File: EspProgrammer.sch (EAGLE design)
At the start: 11 parts

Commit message: add documentation
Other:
- note added: "ESP-12"
- note added: "GPIO0 (with Pull-Up) RESET (with Pull-Up) RXD TXD GND"
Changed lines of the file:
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@@
 <setting verticaltext="up"/>
 </settings>
-<grid distance="0.1" unitdist="inch" unit="inch" style="lines" multiple="1" display="no" altdistance="0.01" altunitdist="inch" altunit="inch"/>
+<grid distance="25" unitdist="mil" unit="mil" style="lines" multiple="1" display="no" altdistance="0.01" altunitdist="inch" altunit="inch"/>
 <layers>
 <layer number="1" name="Top" color="4" fill="1" visible="no" active="no"/>
@@
 <wire x1="116.84" y1="106.68" x2="73.66" y2="106.68" width="0.1524" layer="94"/>
 <text x="78.74" y="93.98" size="1.778" layer="94">CP2104 Board</text>
+<wire x1="182.88" y1="114.3" x2="182.88" y2="99.06" width="0.1524" layer="94"/>
+<wire x1="182.88" y1="88.9" x2="182.88" y2="83.82" width="0.1524" layer="94"/>
+<wire x1="182.88" y1="83.82" x2="210.82" y2="83.82" width="0.1524" layer="94"/>
+<text x="185.42" y="110.49" size="1.778" layer="94">ESP-12</text>
+<text x="184.15" y="87.63" size="1.778" layer="94">GPIO0 (with Pull-Up)
+RESET (with Pull-Up)
+RXD
+TXD
+GND</text>
+<wire x1="180.34" y1="99.06" x2="182.88" y2="99.06" width="0.1524" layer="94"/>
+<wire x1="182.88" y1="99.06" x2="182.88" y2="96.52" width="0.1524" layer="94"/>
+<wire x1="180.34" y1="96.52" x2="182.88" y2="96.52" width="0.1524" layer="94"/>
+<wire x1="182.88" y1="96.52" x2="182.88" y2="93.98" width="0.1524" layer="94"/>
+<wire x1="180.34" y1="93.98" x2="182.88" y2="93.98" width="0.1524" layer="94"/>
+<wire x1="182.88" y1="93.98" x2="182.88" y2="91.44" width="0.1524" layer="94"/>
+<wire x1="180.34" y1="91.44" x2="182.88" y2="91.44" width="0.1524" layer="94"/>
+<wire x1="182.88" y1="91.44" x2="182.88" y2="88.9" width="0.1524" layer="94"/>
+<wire x1="182.88" y1="88.9" x2="180.34" y2="88.9" width="0.1524" layer="94"/>
+<wire x1="182.88" y1="114.3" x2="210.82" y2="114.3" width="0.1524" layer="94"/>
+<wire x1="210.82" y1="114.3" x2="210.82" y2="83.82" width="0.1524" layer="94"/>
 </plain>
 <instances>
@@
 </drawing>
 <compatibility>
+<note version="6.3" minversion="6.2.2" severity="warning">
+Since Version 6.2.2 text objects can contain more than one line,
+which will not be processed correctly with this version.
+</note>
 <note version="8.2" severity="warning">
 Since Version 8.2, EAGLE supports online libraries. The ids

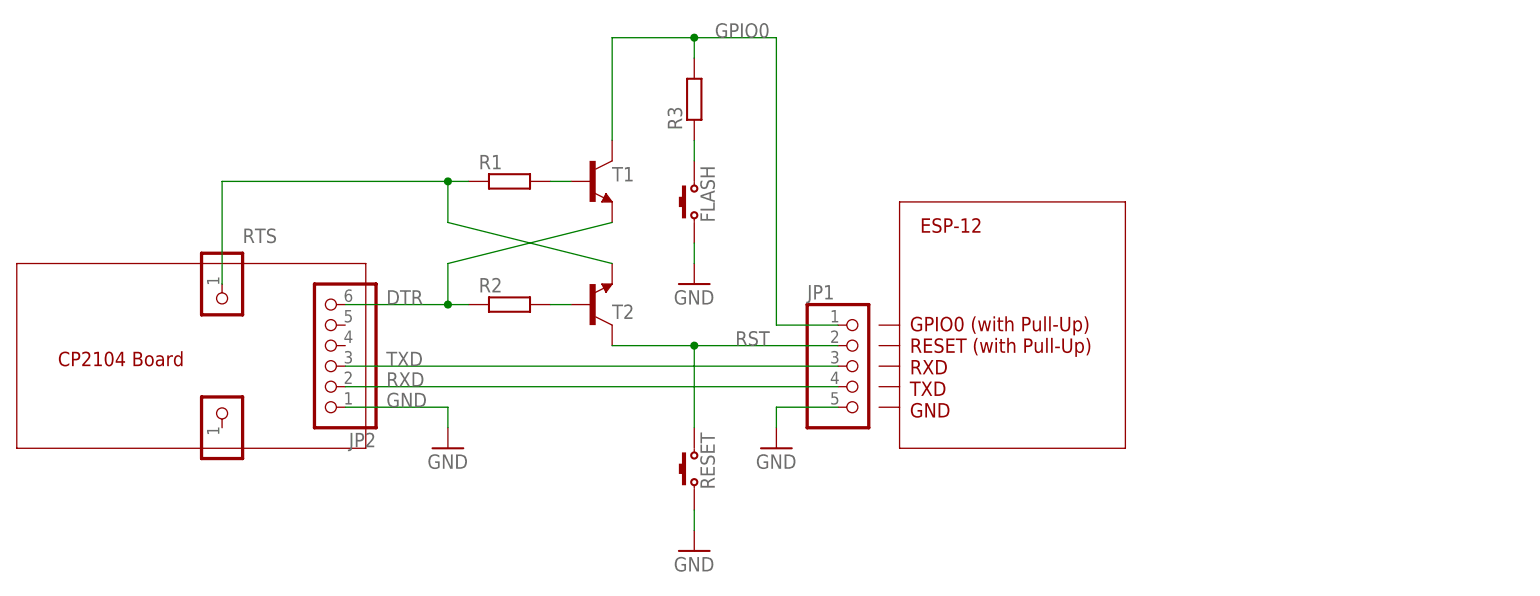
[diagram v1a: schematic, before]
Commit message: change transistor package
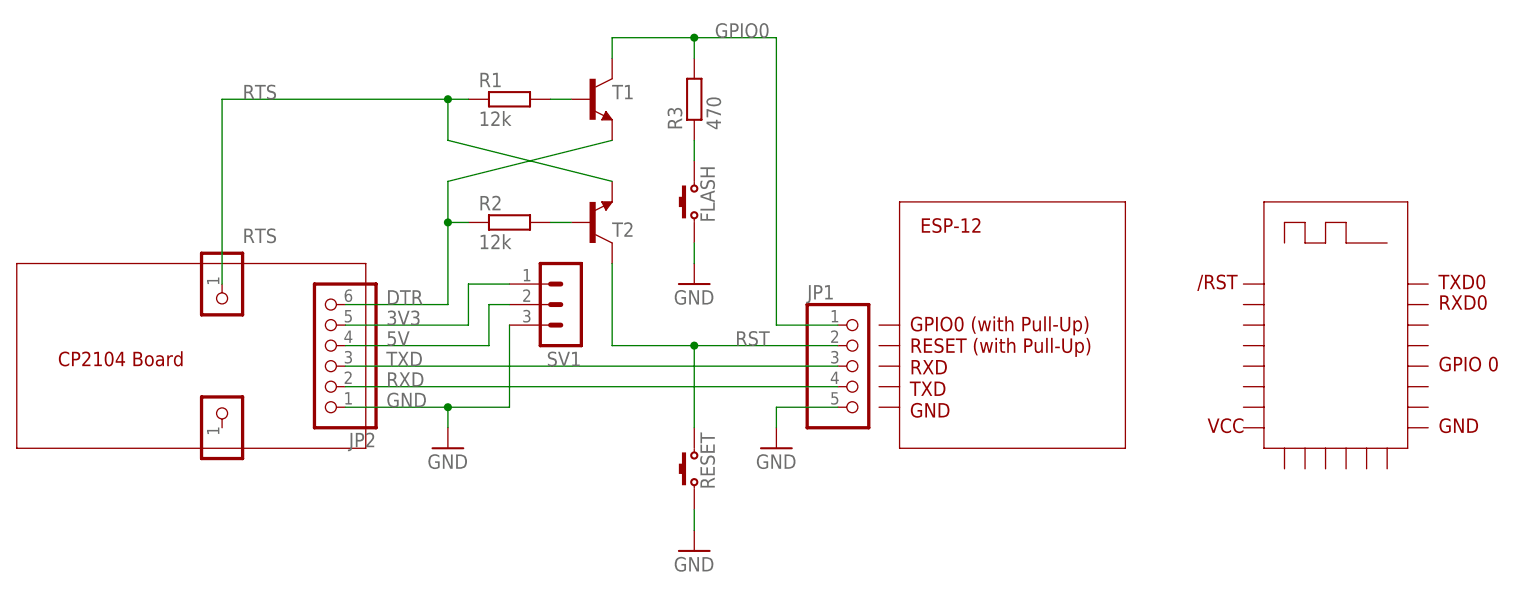
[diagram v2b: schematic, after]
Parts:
- added SV1: (no value), con-lstb:MA03-1
- R1, R2: value (none) -> 12k
- R3: value (none) -> 470
- T1, T2: value (none) -> BC817-40LT1SMD; device transistor:-NPN-SOT23-EBC -> transistor-npn:BC817-40LT1SMD
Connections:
- new net 3V3: JP2.5, SV1.1
- new net 5V: JP2.4, SV1.2
- net GND: now also SV1.3
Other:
- note added: "/RST"
- note added: "GND"
- note added: "GPIO 0"
- note added: "RXD0"
- note added: "TXD0"
- note added: "VCC"
- moved on the sheet: R1, R2, T1, T2
